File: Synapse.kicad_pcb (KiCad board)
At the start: 4 copper layers, 44.4 x 55.2 mm, 5 parts, among them U1 WeAct_BlackPill

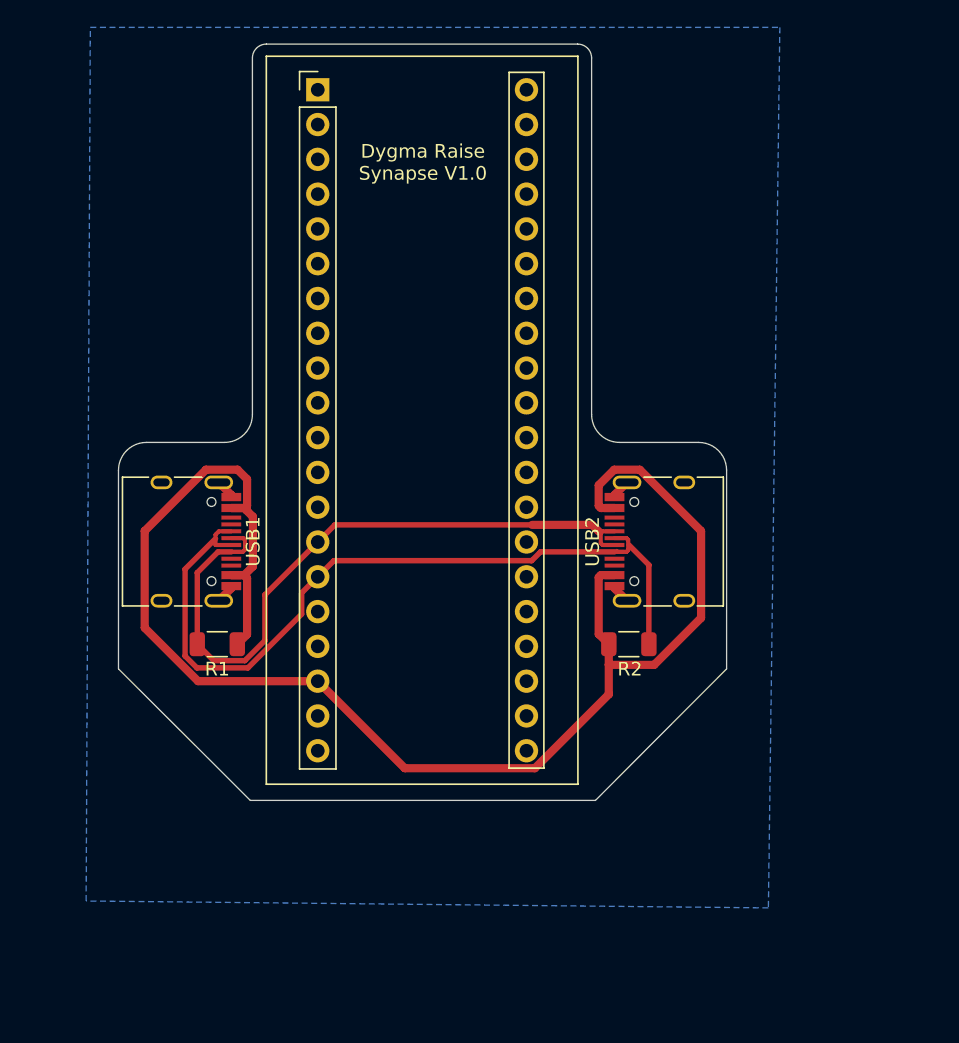
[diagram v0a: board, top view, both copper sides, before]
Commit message: Rebuild the pcb in a cleaner way
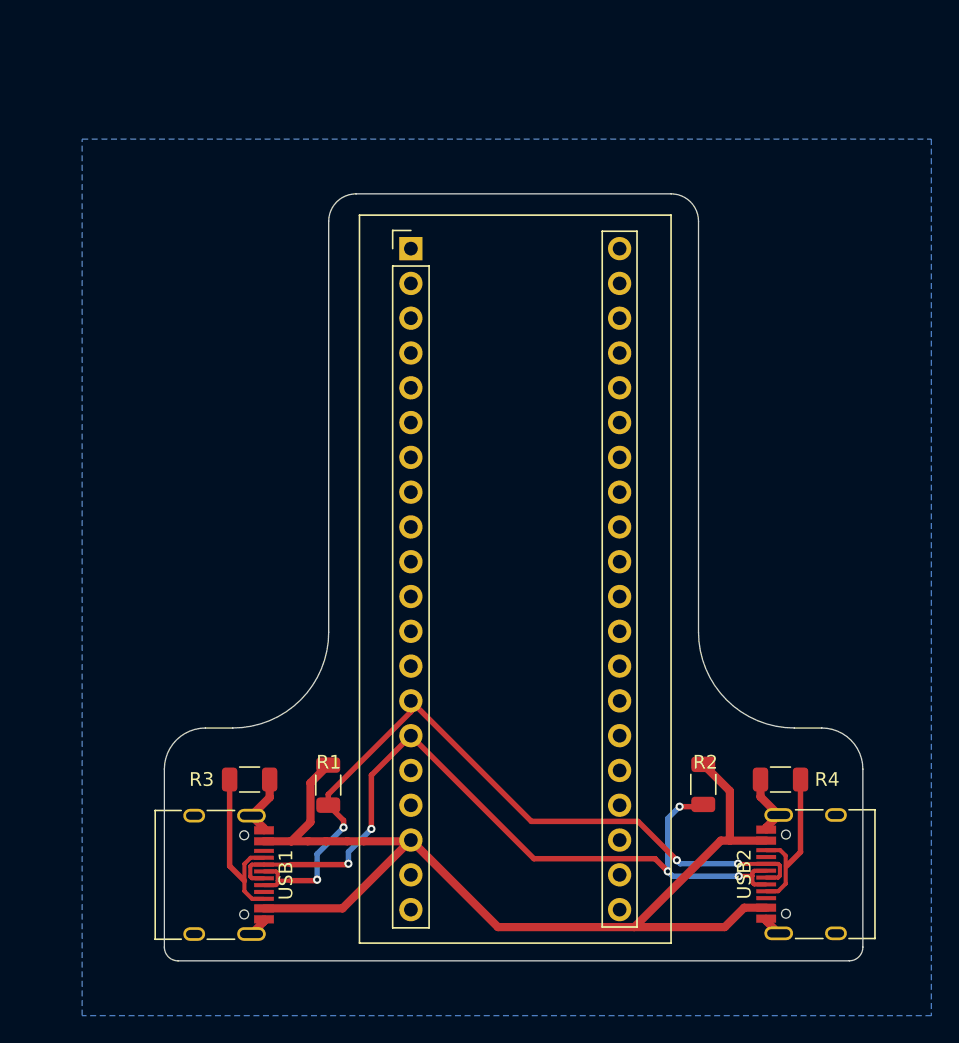
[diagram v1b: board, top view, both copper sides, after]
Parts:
- added R3: 200k, Resistor_SMD:R_1206_3216Metric, F.Cu at (138.2, 73.8)
- added R4: 200k, Resistor_SMD:R_1206_3216Metric, F.Cu at (177.0, 73.8)
- moved USB2 26.7 mm to (180.0, 80.7)
- moved USB1 24.5 mm to (135.2, 80.7)
- moved U1 13.4 mm to (150.0, 35.0)
- moved R1 13.1 mm to (144.0, 74.2), turned to 270 degrees
- moved R2 11.6 mm to (171.3, 74.1), turned to 270 degrees
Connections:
- USB1 pad A5: (no net) -> /cc-1
- USB1 pad B5: (no net) -> /cc-1
- USB2 pad A5: (no net) -> /cc-2
- USB2 pad B5: (no net) -> /cc-2
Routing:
- net /vbus: track 111.1 -> 78.0 mm
- net /cc-1: track 0.00 -> 13.1 mm
- net /cc-2: track 0.00 -> 12.0 mm
- net /gnd: track 5.80 -> 12.1 mm
- net /scl: track 50.1 -> 56.3 mm, vias 0 -> 4
- net /sda: track 59.5 -> 59.2 mm, vias 0 -> 5
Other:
- board size 44.4 x 55.2 mm -> 51 x 56 mm
- copper layers 4 -> 2

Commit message: Use VCC for a top layer
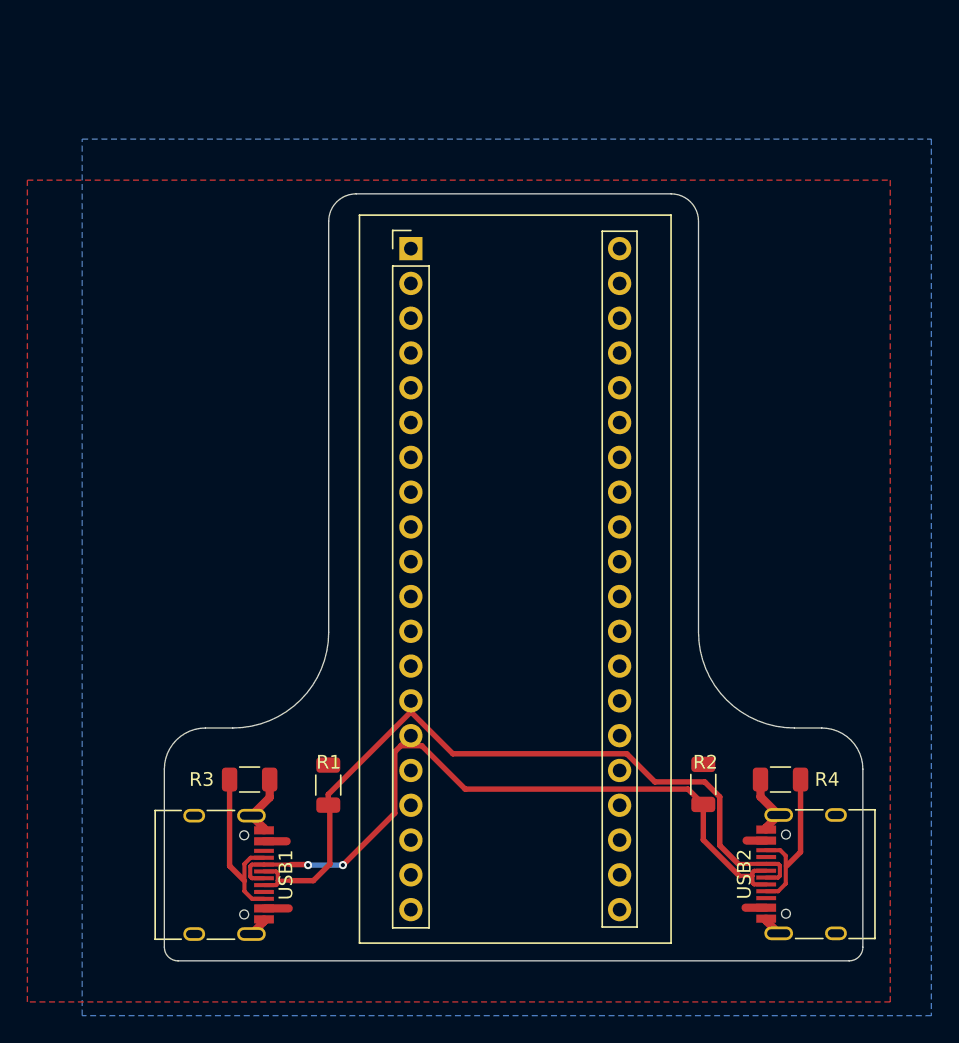
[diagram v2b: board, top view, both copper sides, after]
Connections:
- U1 pad 39: /gnd -> (no net)
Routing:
- net /vbus: track 78.0 -> 6.40 mm
- net /sda: track 59.2 -> 54.1 mm, vias 5 -> 2
- net /scl: vias 4 -> 0
- added copper zone on F.Cu, net /vbus

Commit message: synapse mini
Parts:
- removed U1: WeAct_BlackPill, Footprints:YAAJ_BluePill_2
- added U2: WeAct_BlackPill_Short, Footprints:BlackPill_Short, F.Cu at (150.0, 64.0)
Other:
- board size 51 x 56 mm -> 51 x 23.1 mm

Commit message: PAUSED: Use `git resume` to continue working.
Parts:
- added C1: 100pF ceramic, 100v, 10%, Capacitor_SMD:C_0805_2012Metric, F.Cu at (158.6, 56.9)
- added FB1: Ferrite_Bead_Small, Inductor_SMD:L_0805_2012Metric, F.Cu at (154.2, 52.3)
- added Q1: Q_PMOS_GSD, -3.6A 0.02R, Package_TO_SOT_SMD:SOT-23, F.Cu at (154.2, 55.9)
- added Q2: Q_NMOS_GSD 1Amp, Package_TO_SOT_SMD:SOT-23, F.Cu at (158.7, 53.2)
- added R5: 10k. 125mW. 5%., Resistor_SMD:R_0805_2012Metric, F.Cu at (172.7, 60.4)
- added R6: 10k. 125mW. 5%., Resistor_SMD:R_0805_2012Metric, F.Cu at (163.2, 55.3)
- R1, R2, R3, R4: footprint Resistor_SMD:R_1206_3216Metric -> Resistor_SMD:R_0805_2012Metric
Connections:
- U2 pad 18: /vbus -> +5V
- U2 pad 19: /gnd -> GNDREF
- USB1 pad A1: /gnd -> GNDREF
- USB1 pad A12: /gnd -> GNDREF
- USB1 pad A4: /vbus -> /side-power
- USB1 pad A9: /vbus -> /side-power
- USB1 pad B1: /gnd -> GNDREF
- USB1 pad B12: /gnd -> GNDREF
- USB1 pad B4: /vbus -> /side-power
- USB1 pad B9: /vbus -> /side-power
- USB1 pad S1: /gnd -> GNDREF
- USB2 pad A1: /gnd -> GNDREF
- USB2 pad A12: /gnd -> GNDREF
- USB2 pad A4: /vbus -> /side-power
- USB2 pad A9: /vbus -> /side-power
- USB2 pad B1: /gnd -> GNDREF
- USB2 pad B12: /gnd -> GNDREF
- USB2 pad B4: /vbus -> /side-power
- USB2 pad B9: /vbus -> /side-power
- USB2 pad S1: /gnd -> GNDREF
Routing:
- net GNDREF: track 0.00 -> 12.1 mm
- net /gnd: track 12.1 -> 0.00 mm
- net /vbus: track 6.40 -> 0.00 mm
- net /side-power: track 0.00 -> 6.40 mm
